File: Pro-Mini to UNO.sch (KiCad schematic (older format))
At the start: 8 parts, among them J101 DC 5.5x2.1mm, J102 2pin, U101 ARDUINO_UNOr3, U102 ARDUINO_Pro-Mini

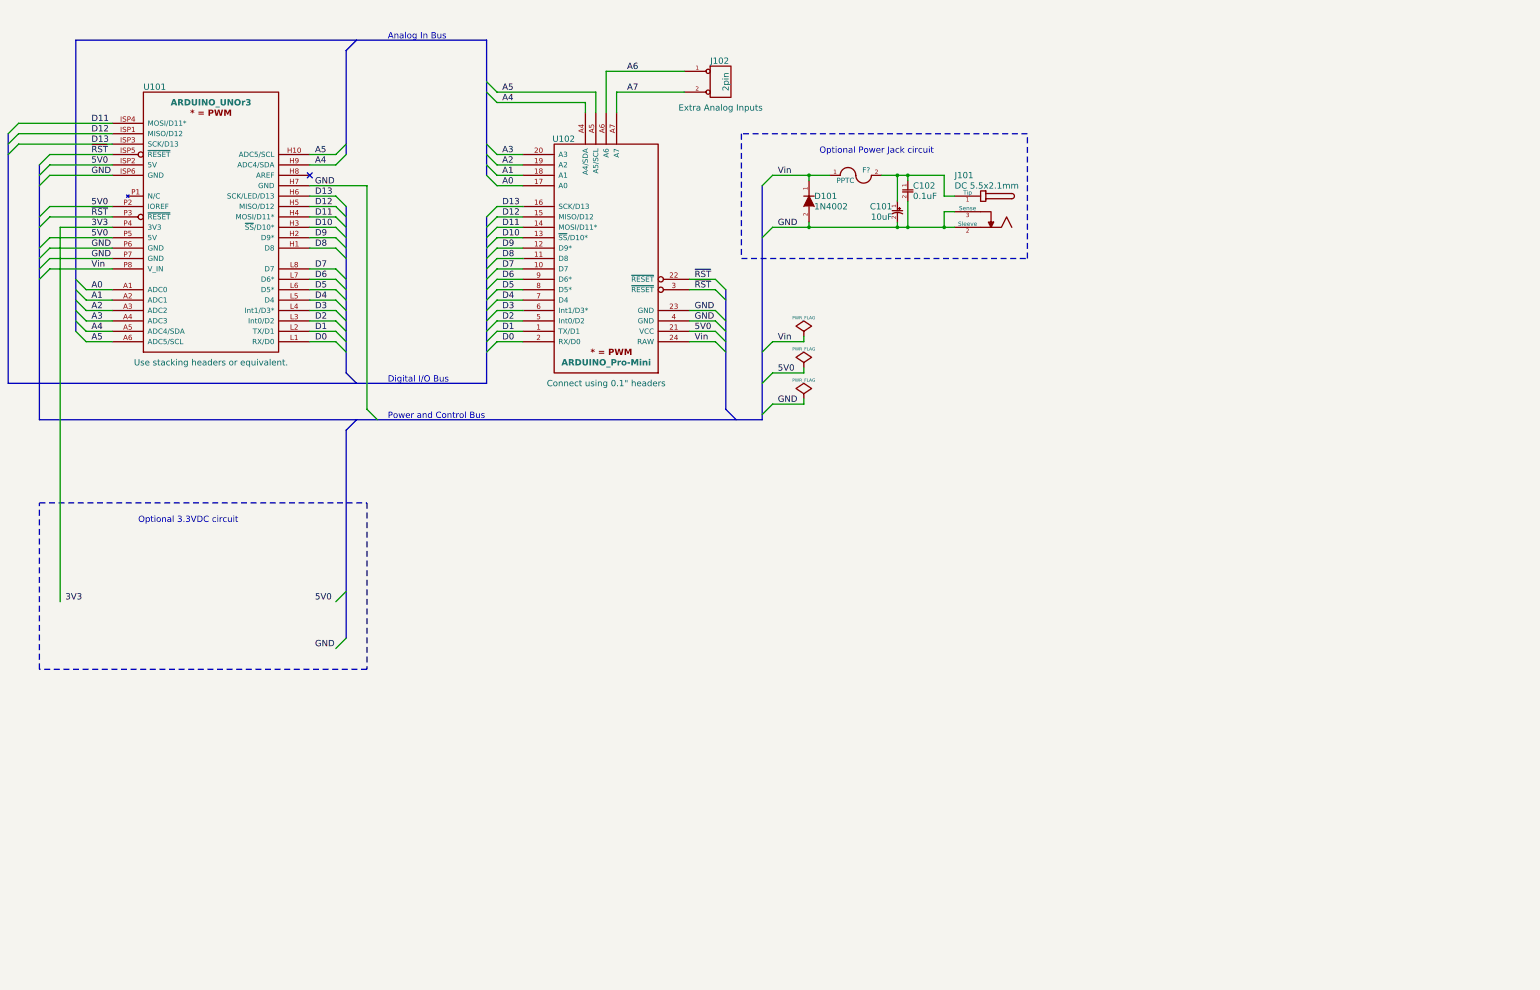
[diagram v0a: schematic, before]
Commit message: Finalize schematic thoughts
Basic concept and power supply options finalized. Still need to add
usage documentation and finalize footprints.
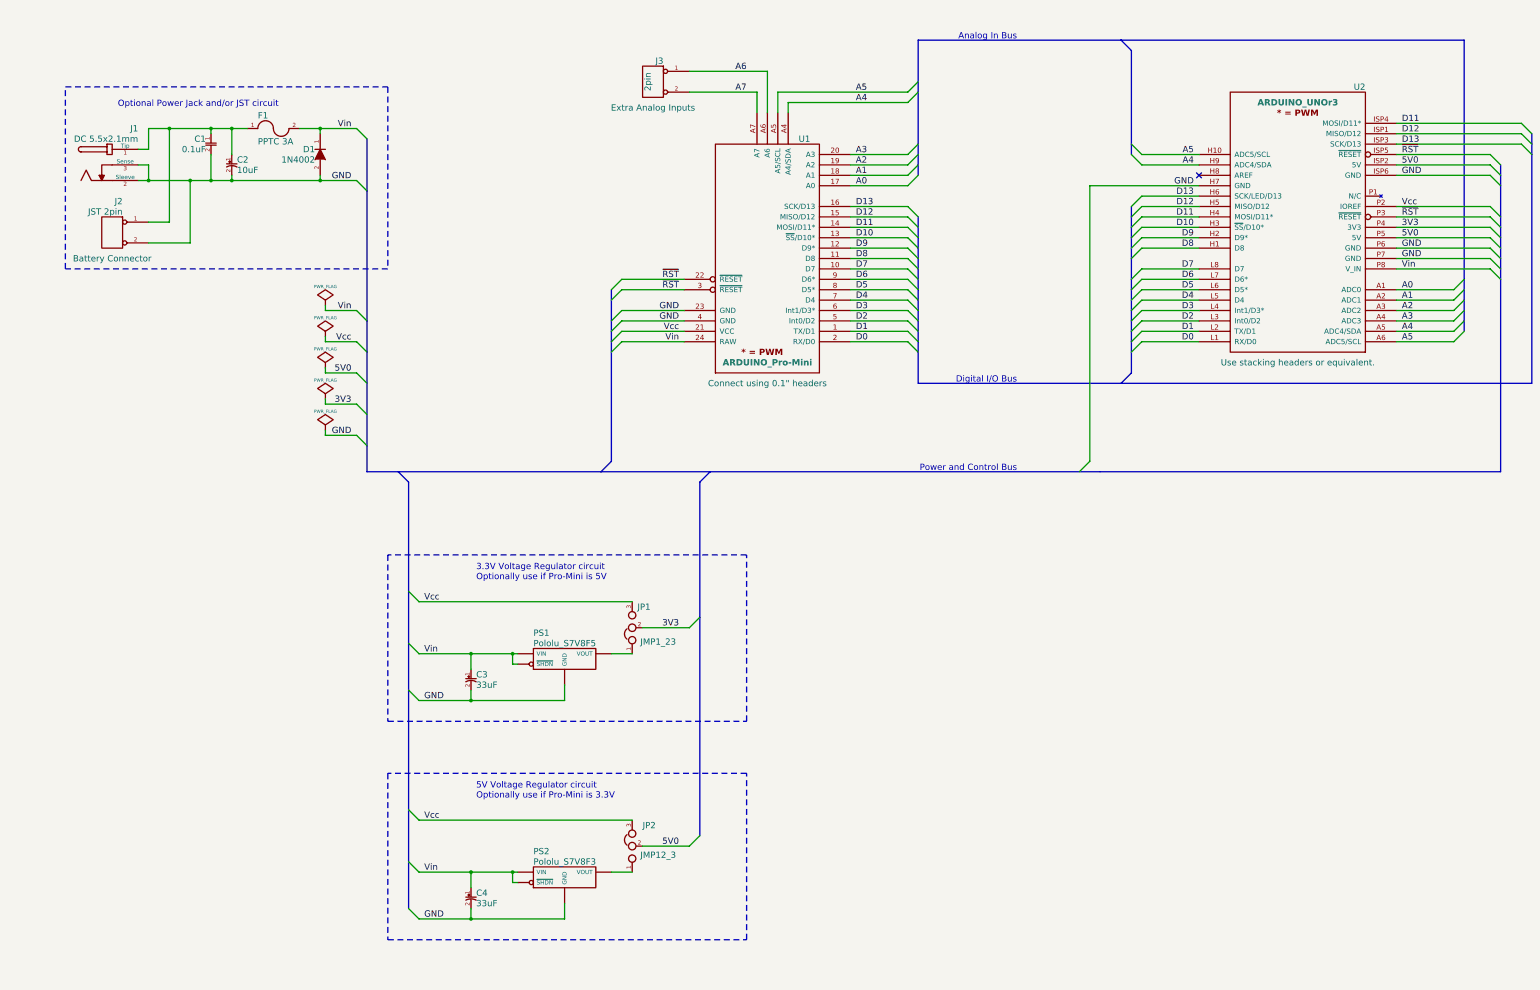
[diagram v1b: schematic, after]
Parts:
- added C3, C4: 33uF, symbol CAP_P
- added J2: JST 2pin, symbol CONN_02
- added JP1: JMP1_23, symbol JMP1_23
- added JP2: JMP12_3, symbol JMP12_3
- added PS1: Pololu_S7V8F5, symbol Pololu_S7V8F5
- added PS2: Pololu_S7V8F3, symbol Pololu_S7V8F3
- F1: renamed from F?; value PPTC -> PPTC 3A
- renumbered C102 to C1, C101 to C2, D101 to D1, J101 to J1, J102 to J3, U102 to U1, U101 to U2
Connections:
- net 3V3: now also JP1.2
- net 5V0: now also JP2.2; no longer U1.21 (VCC), U2.P2 (IOREF)
- net GND: now also C3.2, C4.2, J2.2, PS1.GND, PS2.GND
- net Vin: now also F1.2, C3.1, C4.1, PS1.VIN, PS1.~SHD (~SHDN), PS2.VIN, PS2.~SHD (~SHDN); no longer F1.1
- net at C1.1, C2.1, J1.1 (Tip): now also F1.1, J2.1; no longer F1.2
- new net: JP2.1, PS2.VOUT
- new net: JP1.1, PS1.VOUT
- new net Vcc: JP1.3, JP2.3, U1.21 (VCC), U2.P2 (IOREF)
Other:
- note added: "3.3V Voltage Regulator circuit\nOptionally use if Pro-Mini is 5V"
- note added: "5V Voltage Regulator circuit\nOptionally use if Pro-Mini is 3.3V"
- note added: "Optional Power Jack and/or JST circuit"
- note removed: "Optional 3.3VDC circuit"
- note removed: "Optional Power Jack circuit"
- moved on the sheet: C1, C2, D1, F1, J1, J3, U1, U2

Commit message: Regulator correction
Corrected regulator positioning (had them reversed) and started on usage
comments.
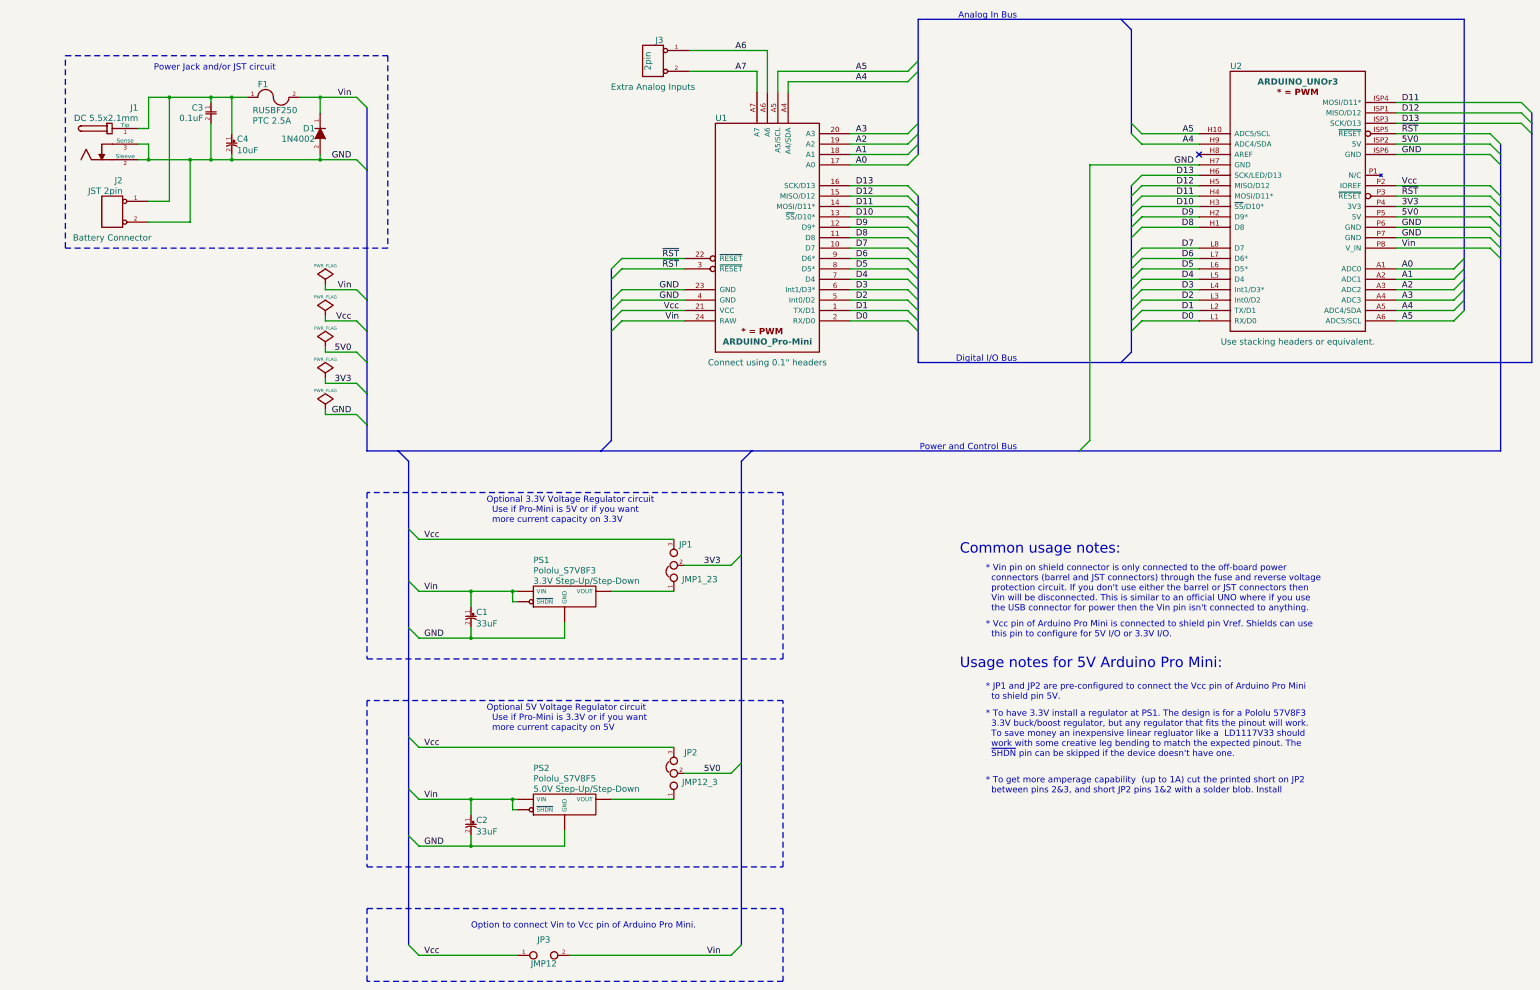
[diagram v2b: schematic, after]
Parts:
- added JP3: JMP12, symbol JMP12
- F1: value PPTC 3A -> RUSBF250; Detail (none) -> PTC 2.5A; URL (none) -> https://octopart.com/search?view=list&q=RUSBF250
- PS1: renamed from PS2; Detail (none) -> 3.3V Step-Up/Step-Down
- PS2: renamed from PS1; Detail (none) -> 5.0V Step-Up/Step-Down
- renumbered C3 to C1, C4 to C2, C1 to C3, C2 to C4
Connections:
- net Vcc: now also JP3.1
- net Vin: now also JP3.2
- net at JP2.1: now also PS2.VOUT; no longer PS1.VOUT
- net at JP1.1: now also PS1.VOUT; no longer PS2.VOUT
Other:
- note added: "* JP1 and JP2 are pre-configured to connect the Vcc pin of Arduino Pro Mini\n to shield pin 5V."
- note added: "* To get more amperage capability (up to 1A) cut the printed short on JP2\n between pins 2&3, and short JP2 pins 1&2 with a solder blob. Install"
- note added: "* To have 3.3V install a regulator at PS1. The design is for a Pololu 57V8F3\n 3.3V buck/boost regulator, but any regulator that fits the pinout will work.\n To save money an inexpensive linear regluator like a LD1117V33 should\n work with some creative leg bending to match the expected pinout. The\n ~SHDN~ pin can be skipped if the device doesn't have one."
- note added: "* Vcc pin of Arduino Pro Mini is connected to shield pin Vref. Shields can use\n this pin to configure for 5V I/O or 3.3V I/O."
- note added: "* Vin pin on shield connector is only connected to the off-board power\n connectors (barrel and JST connectors) through the fuse and reverse voltage\n protection circuit. If you don't use either the barrel or JST connectors then\n Vin will be disconnected. This is similar to an official UNO where if you use\n the USB connector for power then the Vin pin isn't connected to anything."
- note added: "Common usage notes:"
- note added: "Option to connect Vin to Vcc pin of Arduino Pro Mini."
- note added: "Optional 3.3V Voltage Regulator circuit\n Use if Pro-Mini is 5V or if you want\n more current capacity on 3.3V"
- note added: "Optional 5V Voltage Regulator circuit\n Use if Pro-Mini is 3.3V or if you want\n more current capacity on 5V"
- note added: "Power Jack and/or JST circuit"
- note added: "Usage notes for 5V Arduino Pro Mini:"
- note removed: "3.3V Voltage Regulator circuit\nOptionally use if Pro-Mini is 5V"
- note removed: "5V Voltage Regulator circuit\nOptionally use if Pro-Mini is 3.3V"
- note removed: "Optional Power Jack and/or JST circuit"
- moved on the sheet: C1, C2, C3, C4, D1, F1, J1, J2, J3, JP1, JP2, PS1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

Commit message: collected updates
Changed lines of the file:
@@
 	14000 1800 15200 1800
 Wire Bus Line
-	11450 2600 11450 2700
+	11450 2600 11450 4200
 Wire Bus Line
-	11450 2700 11450 2800
+	9400 2700 9400 4300
 Wire Bus Line
-	11450 2800 11450 2900
+	9400 1000 9400 2300
 Wire Bus Line
-	11450 2900 11450 3000
+	9400 1000 14650 1000
 Wire Bus Line
-	11450 3000 11450 3100
+	14650 1000 14650 3800
 Wire Bus Line
-	11450 3100 11450 3300
+	11450 1100 11450 2100
 Wire Bus Line
-	11450 3300 11450 3400
+	15300 4300 9400 4300
 Wire Bus Line
-	11450 3400 11450 3500
+	15300 1900 15300 4300
 Wire Bus Line
-	11450 3500 11450 3600
+	4100 5150 15000 5150
 Wire Bus Line
-	11450 3600 11450 3700
-Wire Bus Line
-	11450 3700 11450 3800
-Wire Bus Line
-	11450 3800 11450 3900
-Wire Bus Line
-	11450 3900 11450 4000
-Wire Bus Line
-	11450 4000 11450 4200
-Wire Bus Line
-	9400 2700 9400 2800
-Wire Bus Line
-	9400 2800 9400 2900
-Wire Bus Line
-	9400 2900 9400 3000
-Wire Bus Line
-	9400 3000 9400 3100
-Wire Bus Line
-	9400 3100 9400 3200
-Wire Bus Line
-	9400 3200 9400 3300
-Wire Bus Line
-	9400 3300 9400 3400
-Wire Bus Line
-	9400 3400 9400 3500
-Wire Bus Line
-	9400 3500 9400 3600
-Wire Bus Line
-	9400 3600 9400 3700
-Wire Bus Line
-	9400 3700 9400 3800
-Wire Bus Line
-	9400 3800 9400 3900
-Wire Bus Line
-	9400 3900 9400 4000
-Wire Bus Line
-	9400 4000 9400 4300
-Wire Bus Line
-	9400 1000 9400 1400
-Wire Bus Line
-	9400 1400 9400 1500
-Wire Bus Line
-	9400 1500 9400 2000
-Wire Bus Line
-	9400 2000 9400 2100
-Wire Bus Line
-	9400 2100 9400 2200
-Wire Bus Line
-	9400 2200 9400 2300
-Wire Bus Line
-	9400 1000 11350 1000
-Wire Bus Line
-	11350 1000 14650 1000
-Wire Bus Line
-	14650 1000 14650 3300
-Wire Bus Line
-	14650 3300 14650 3400
-Wire Bus Line
-	14650 3400 14650 3500
-Wire Bus Line
-	14650 3500 14650 3600
-Wire Bus Line
-	14650 3600 14650 3700
-Wire Bus Line
-	14650 3700 14650 3800
-Wire Bus Line
-	11450 1100 11450 2000
-Wire Bus Line
-	11450 2000 11450 2100
-Wire Bus Line
-	15300 4300 11350 4300
-Wire Bus Line
-	11350 4300 9400 4300
-Wire Bus Line
-	15300 1900 15300 2000
-Wire Bus Line
-	15300 2000 15300 2100
-Wire Bus Line
-	15300 2100 15300 4300
-Wire Bus Line
-	4100 5150 4400 5150
-Wire Bus Line
-	4400 5150 6350 5150
-Wire Bus Line
-	6350 5150 7800 5150
-Wire Bus Line
-	7800 5150 10950 5150
-Wire Bus Line
-	10950 5150 15000 5150
-Wire Bus Line
-	15000 2200 15000 2300
-Wire Bus Line
-	15000 2300 15000 2400
-Wire Bus Line
-	15000 2400 15000 2700
-Wire Bus Line
-	15000 2700 15000 2800
-Wire Bus Line
-	15000 2800 15000 2900
-Wire Bus Line
-	15000 2900 15000 3000
-Wire Bus Line
-	15000 3000 15000 3100
-Wire Bus Line
-	15000 3100 15000 3200
-Wire Bus Line
-	15000 3200 15000 3300
-Wire Bus Line
-	15000 3300 15000 5150
+	15000 2200 15000 5150
 Wire Wire Line
 	7200 1300 7950 1300
@@
 	7850 1500 7850 1700
 Wire Wire Line
-	1900 2350 2000 2350
-Wire Wire Line
-	2000 2350 2400 2350
-Wire Wire Line
-	2400 2350 2600 2350
-Wire Wire Line
-	2600 2350 2800 2350
-Wire Wire Line
-	2800 2350 3650 2350
-Wire Wire Line
-	3650 2350 4000 2350
+	1900 2350 4000 2350
 Wire Bus Line
-	4100 1850 4100 2450
+	4100 1850 4100 5150
 Wire Bus Line
-	4100 2450 4100 3700
-Wire Bus Line
-	4100 3700 4100 4000
-Wire Bus Line
-	4100 4000 4100 4300
-Wire Bus Line
-	4100 4300 4100 4600
-Wire Bus Line
-	4100 4600 4100 4900
-Wire Bus Line
-	4100 4900 4100 5150
-Wire Bus Line
-	6450 3400 6450 3500
-Wire Bus Line
-	6450 3500 6450 3700
-Wire Bus Line
-	6450 3700 6450 3800
-Wire Bus Line
-	6450 3800 6450 3900
-Wire Bus Line
-	6450 3900 6450 4000
-Wire Bus Line
-	6450 4000 6450 5050
+	6450 3400 6450 5050
 Wire Wire Line
 	3700 4450 3700 4500
@@
 	14000 2800 14900 2800
 Wire Bus Line
-	4500 5250 4500 5900
-Wire Bus Line
-	4500 5900 4500 6400
-Wire Bus Line
-	4500 6400 4500 6850
-Wire Bus Line
-	4500 6850 4500 7900
-Wire Bus Line
-	4500 7900 4500 8400
-Wire Bus Line
-	4500 8400 4500 8850
-Wire Bus Line
-	4500 8850 4500 9900
+	4500 5250 4500 9900
 Wire Wire Line
 	11050 2400 11050 5050
 Wire Wire Line
-	3450 1750 3650 1750
+	3450 1750 4000 1750
 Wire Wire Line
-	3650 1750 4000 1750
-Wire Wire Line
-	2000 1750 2200 1750
-Wire Wire Line
-	2200 1750 2600 1750
-Wire Wire Line
-	2600 1750 2800 1750
-Wire Wire Line
-	2800 1750 2950 1750
+	2000 1750 2950 1750
 Wire Wire Line
 	2000 1750 2000 2050
@@
 Connection ~ 2400 2350
 Wire Wire Line
-	4600 6950 5100 6950
-Wire Wire Line
-	5100 6950 6000 6950
+	4600 6950 6000 6950
 Wire Wire Line
 	6000 6950 6000 6800
@@
 	8100 7150 8100 5550
 Wire Wire Line
-	4600 8950 5100 8950
-Wire Wire Line
-	5100 8950 6000 8950
+	4600 8950 6000 8950
 Wire Wire Line
 	6000 8950 6000 8800
 Wire Wire Line
-	4600 8500 5100 8500
-Wire Wire Line
-	5100 8500 5500 8500
-Wire Wire Line
-	5500 8500 5550 8500
+	4600 8500 5550 8500
 Wire Wire Line
 	5550 8600 5500 8600
@@
 Connection ~ 5100 8950
 Wire Wire Line
-	4600 6500 5100 6500
-Wire Wire Line
-	5100 6500 5500 6500
-Wire Wire Line
-	5500 6500 5550 6500
+	4600 6500 5550 6500
 Wire Wire Line
 	7050 8000 4600 8000
@@
 	6550 3800 6450 3900
 Wire Bus Line
-	7700 5250 7700 6150
-Wire Bus Line
-	7700 6150 7700 8150
-Wire Bus Line
-	7700 8150 7700 9900
+	7700 5250 7700 9900
 Entry Bus Bus
 	7700 5250 7800 5150
